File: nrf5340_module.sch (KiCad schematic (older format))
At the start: 42 parts, among them J1 U.FL_A-1JB, U1 nrf5340, Y1 32.768kHz, Y2 32MHz

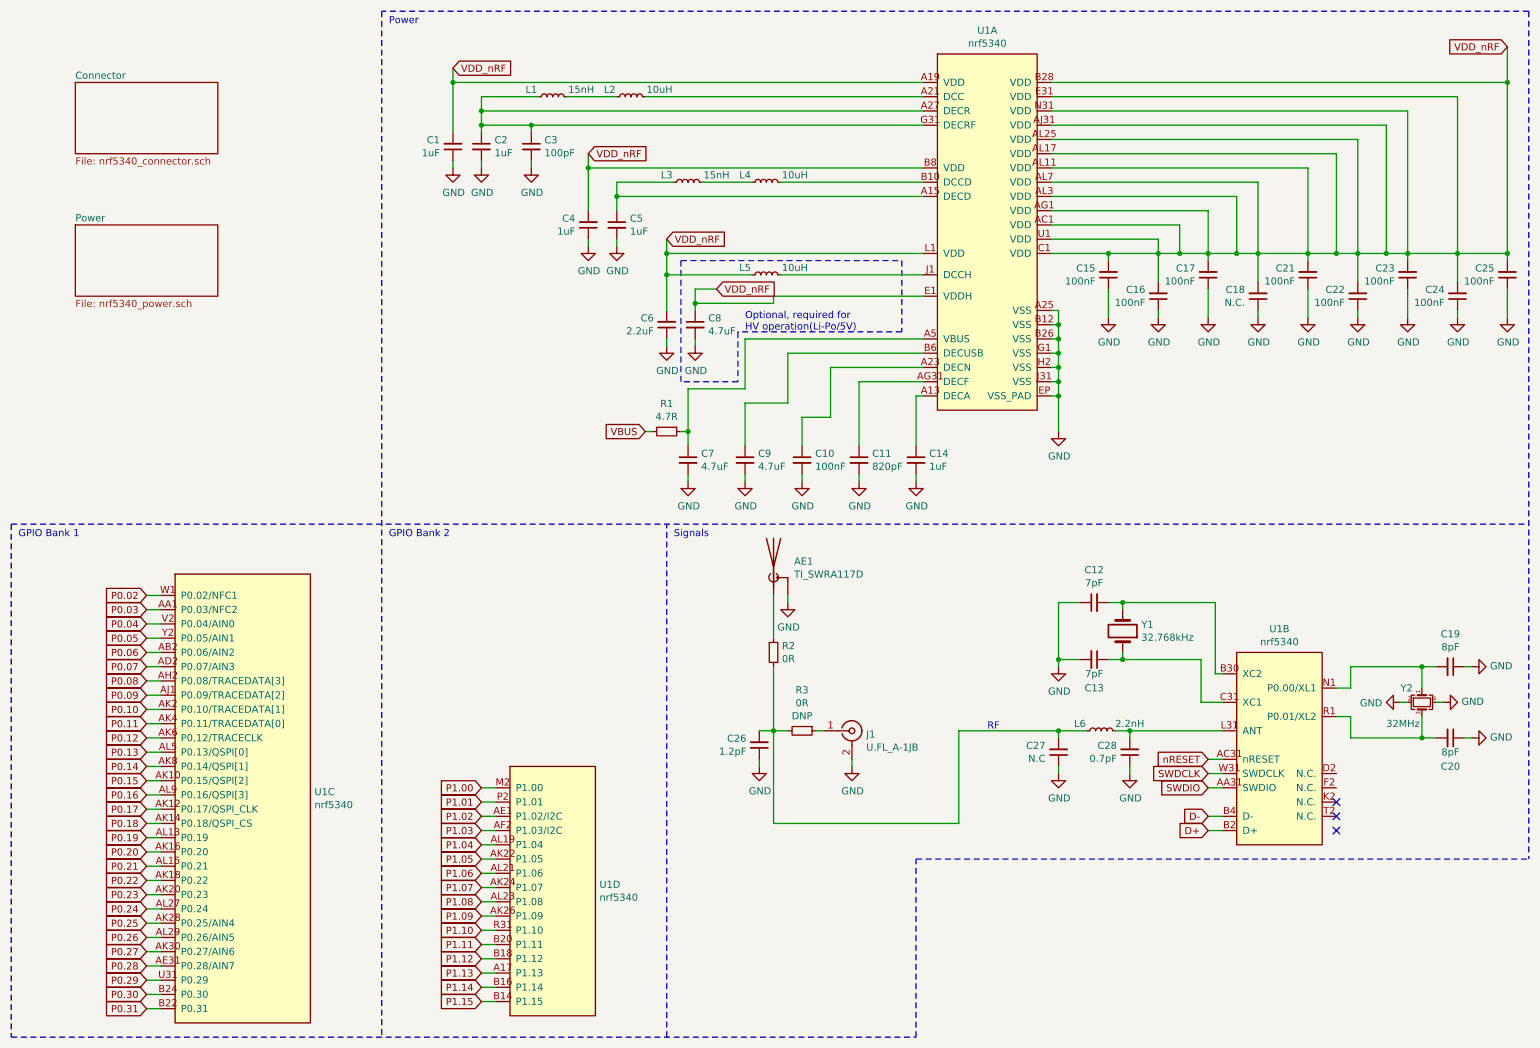
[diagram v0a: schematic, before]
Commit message: first rev pcb without impedance matching
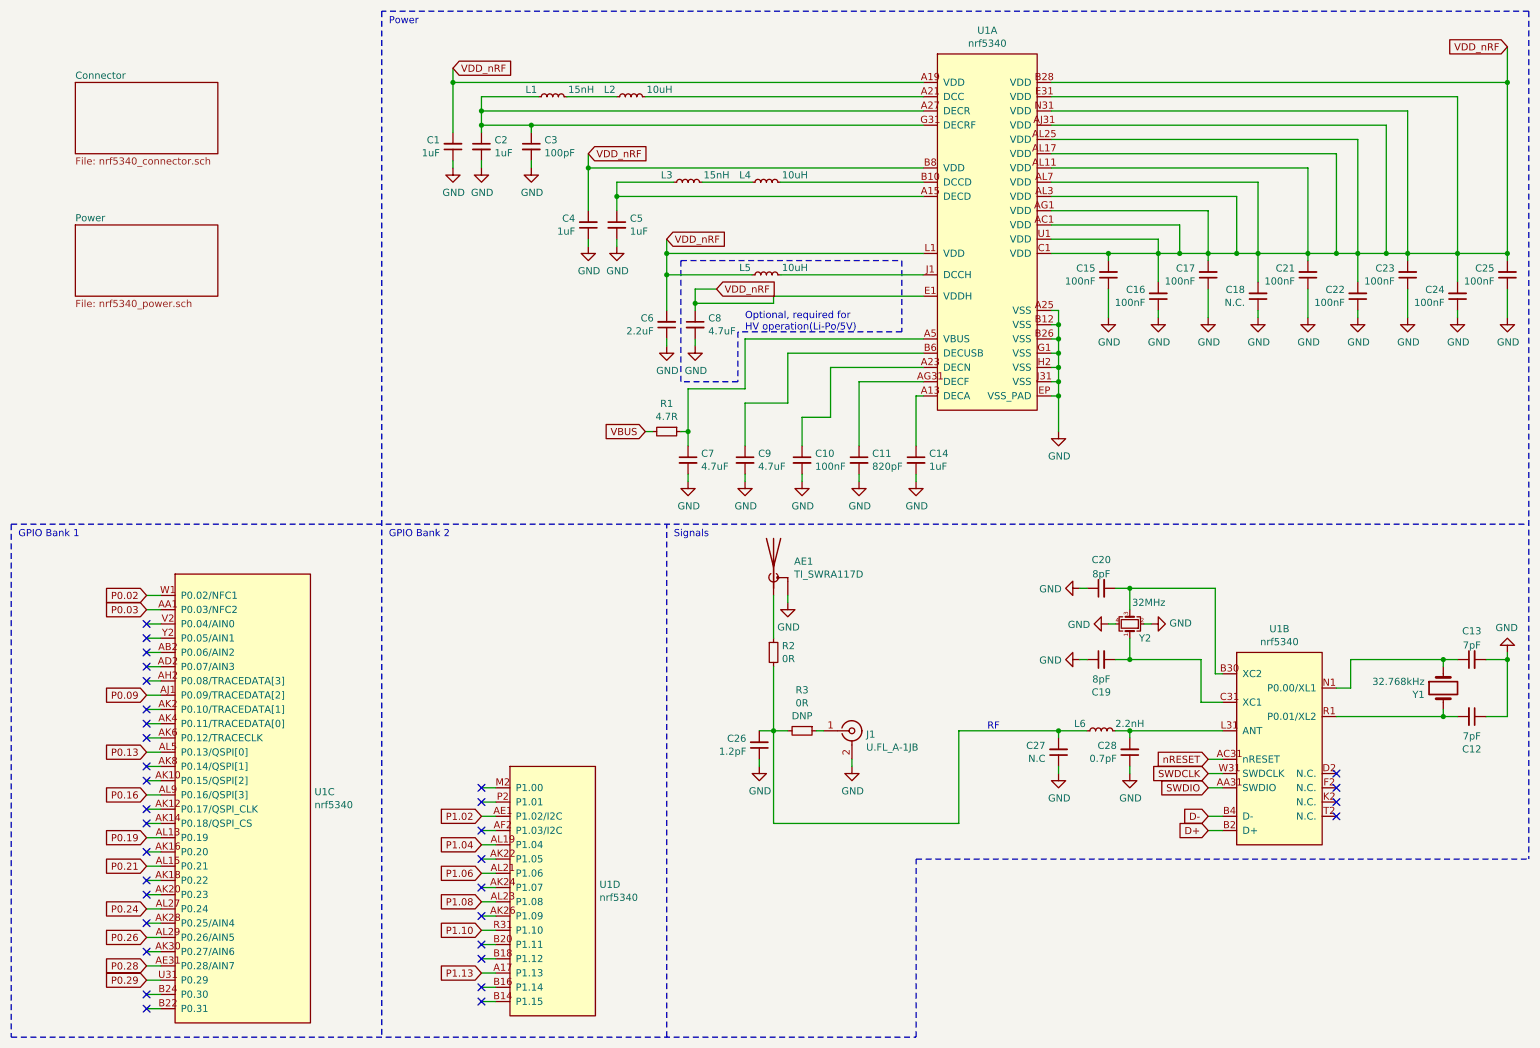
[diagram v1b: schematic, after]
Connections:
- net at C12.2, Y1.2: now also U1.R1 (P0.01/XL2); no longer U1.B30 (XC2)
- net at C13.1, Y1.1: now also U1.N1 (P0.00/XL1); no longer U1.C31 (XC1)
- net at C19.2, Y2.1: now also U1.C31 (XC1); no longer U1.N1 (P0.00/XL1)
- net at C20.2, Y2.3: now also U1.B30 (XC2); no longer U1.R1 (P0.01/XL2)
- net P0.04: no longer names the net of U1.V2 (P0.04/AIN0)
- net P0.05: no longer names the net of U1.Y2 (P0.05/AIN1)
- net P0.06: no longer names the net of U1.AB2 (P0.06/AIN2)
- net P0.07: no longer names the net of U1.AD2 (P0.07/AIN3)
- net P0.08: no longer names the net of U1.AH2 (P0.08/TRACEDATA[3])
- net P0.10: no longer names the net of U1.AK2 (P0.10/TRACEDATA[1])
- net P0.11: no longer names the net of U1.AK4 (P0.11/TRACEDATA[0])
- net P0.12: no longer names the net of U1.AK6 (P0.12/TRACECLK)
- net P0.14: no longer names the net of U1.AK8 (P0.14/QSPI[1])
- net P0.15: no longer names the net of U1.AK10 (P0.15/QSPI[2])
- net P0.17: no longer names the net of U1.AK12 (P0.17/QSPI_CLK)
- net P0.18: no longer names the net of U1.AK14 (P0.18/QSPI_CS)
- net P0.20: no longer names the net of U1.AK16 (P0.20)
- net P0.22: no longer names the net of U1.AK18 (P0.22)
- net P0.23: no longer names the net of U1.AK20 (P0.23)
- net P0.25: no longer names the net of U1.AK28 (P0.25/AIN4)
- net P0.27: no longer names the net of U1.AK30 (P0.27/AIN6)
- net P0.30: no longer names the net of U1.B24 (P0.30)
- net P0.31: no longer names the net of U1.B22 (P0.31)
- net P1.00: no longer names the net of U1.M2 (P1.00)
- net P1.01: no longer names the net of U1.P2 (P1.01)
- net P1.03: no longer names the net of U1.AF2 (P1.03/I2C)
- net P1.05: no longer names the net of U1.AK22 (P1.05)
- net P1.07: no longer names the net of U1.AK24 (P1.07)
- net P1.09: no longer names the net of U1.AK26 (P1.09)
- net P1.11: no longer names the net of U1.B20 (P1.11)
- net P1.12: no longer names the net of U1.B18 (P1.12)
- net P1.14: no longer names the net of U1.B16 (P1.14)
- net P1.15: no longer names the net of U1.B14 (P1.15)
- no-connect marks 3 -> 33
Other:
- moved on the sheet: C12, C13, C19, C20, Y1, Y2

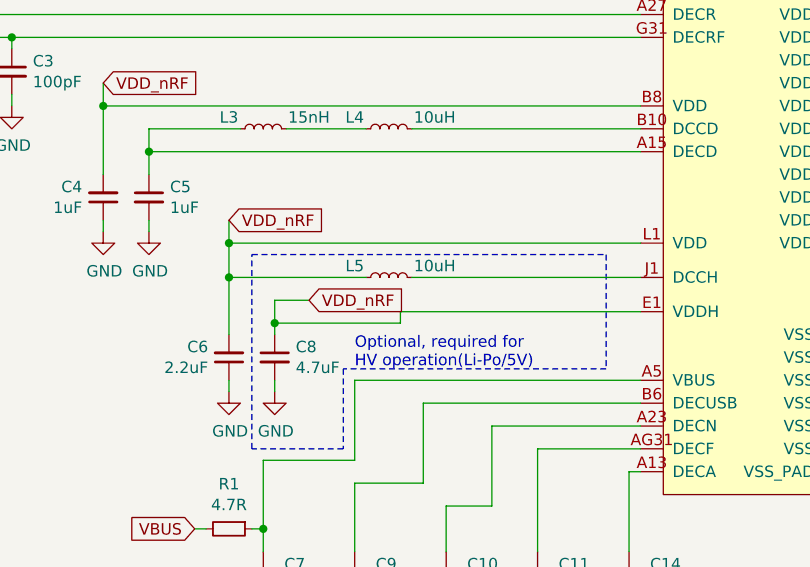
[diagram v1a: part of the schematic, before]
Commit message: fix traces underneath nrf gnd pad and VDD_HV
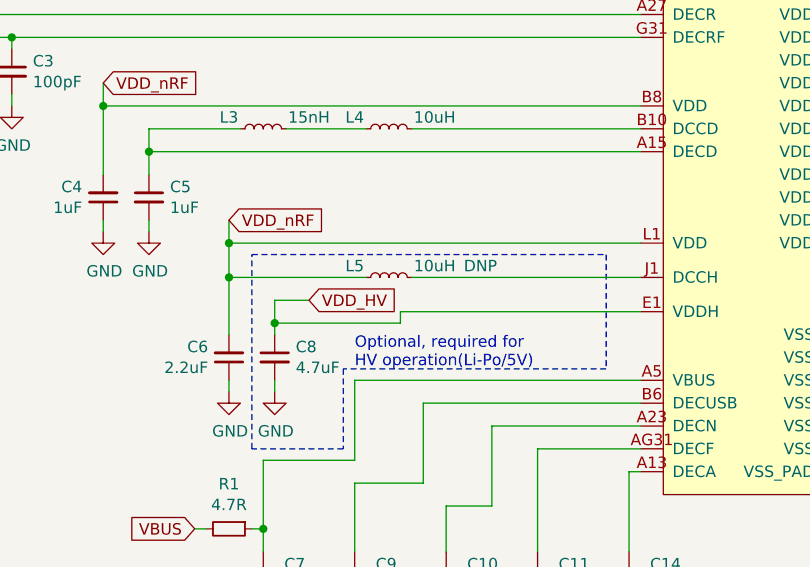
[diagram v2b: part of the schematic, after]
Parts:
- L5: DNP (none) -> DNP
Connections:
- net VDD_nRF: no longer C8.1, U1.E1 (VDDH)
- new net VDD_HV: C8.1, U1.E1 (VDDH)
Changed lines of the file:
@@
 EESchema Schematic File Version 4
+LIBS:nrf5340_module-cache
 EELAYER 30 0
 EELAYER END
@@
 F 2 "Inductor_SMD:L_0603_1608Metric" H 5850 2350 50  0001 C CNN
 F 3 "~" H 5850 2350 50  0001 C CNN
+F 4 "DNP" V 5900 1950 50  0000 C CNN "DNP"
 	1    5850 2350
 	0    -1   -1   0
@@
 Connection ~ 5150 2350
 Text GLabel 5500 2450 2    50   Input ~ 0
-VDD_nRF
+VDD_HV
 Wire Wire Line
 	5500 2450 5350 2450

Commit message: update
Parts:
- removed C8: 4.7uF, Capacitor_SMD:C_0603_1608Metric, symbol Device:C_Small
- added R7: 0R, Resistor_SMD:R_0603_1608Metric, symbol Device:R_Small
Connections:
- net VDD_nRF: now also R7.2
- net VDD_HV: no longer names the net of U1.E1 (VDDH)
- net VDD_HV: now also R7.1
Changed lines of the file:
@@
 EESchema Schematic File Version 4
-LIBS:nrf5340_module-cache
 EELAYER 30 0
 EELAYER END
@@
 Title "nrf5340_module"
 Date "2019-11-17"
-Rev "1.0.0"
+Rev "1.0"
 Comp ""
 Comment1 ""
@@
 $EndComp
 $Comp
-L Device:C_Small C8
-U 1 1 5DDBE086
-P 5350 2700
-F 0 "C8" H 5442 2746 50  0000 L CNN
-F 1 "4.7uF" H 5442 2655 50  0000 L CNN
-F 2 "Capacitor_SMD:C_0603_1608Metric" H 5350 2700 50  0001 C CNN
-F 3 "~" H 5350 2700 50  0001 C CNN
-	1    5350 2700
-	1    0    0    -1
-$EndComp
-$Comp
 L power:GND #PWR0106
 U 1 1 5DDBE08C
@@
 	1    0    0    -1
 $EndComp
-$Comp
-L power:GND #PWR0107
-U 1 1 5DDBE092
-P 5350 2850
-F 0 "#PWR0107" H 5350 2600 50  0001 C CNN
-F 1 "GND" H 5355 2677 50  0000 C CNN
-F 2 "" H 5350 2850 50  0001 C CNN
-F 3 "" H 5350 2850 50  0001 C CNN
-	1    5350 2850
-	1    0    0    -1
-$EndComp
-Wire Wire Line
-	5350 2800 5350 2850
 Wire Wire Line
 	5150 2800 5150 2850
@@
 	5950 2350 6950 2350
 Wire Wire Line
-	5750 2350 5150 2350
+	5750 2350 5350 2350
 Connection ~ 5150 2350
-Text GLabel 5500 2450 2    50   Input ~ 0
-VDD_HV
-Wire Wire Line
-	5500 2450 5350 2450
-Wire Wire Line
-	5350 2450 5350 2550
-Wire Wire Line
-	5350 2550 5900 2550
-Wire Wire Line
-	5900 2550 5900 2500
-Wire Wire Line
-	5900 2500 6950 2500
-Connection ~ 5350 2550
-Wire Wire Line
-	5350 2550 5350 2600
 Wire Wire Line
 	5150 2350 5150 2600
@@
 NoConn ~ 3850 7450
 NoConn ~ 1500 5500
+$Comp
+L Device:R_Small R7
+U 1 1 602574E0
+P 5500 2500
+F 0 "R7" V 5214 2500 50  0000 C CNN
+F 1 "0R" V 5305 2500 50  0000 C CNN
+F 2 "Resistor_SMD:R_0603_1608Metric" H 5500 2500 50  0001 C CNN
+F 3 "~" H 5500 2500 50  0001 C CNN
+F 4 "DNP" V 5396 2500 50  0000 C CNN "DNP"
+	1    5500 2500
+	0    1    -1   0
+$EndComp
+Wire Wire Line
+	5600 2500 6950 2500
+Wire Wire Line
+	5400 2500 5350 2500
+Wire Wire Line
+	5350 2500 5350 2350
+Connection ~ 5350 2350
+Wire Wire Line
+	5350 2350 5150 2350
 $EndSCHEMATC
